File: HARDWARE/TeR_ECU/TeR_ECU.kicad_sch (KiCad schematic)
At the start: 6 parts

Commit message: Quick changes
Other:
- removed sheet ShutdownCircuit
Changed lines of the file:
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@@
-		)
-	)
-	(wire
-		(pts
-			(xy 83.82 149.86) (xy 83.82 151.13)
-		)
-		(stroke
-			(width 0)
-			(type default)
 		)
 	)
@@
 		(pts
 			(xy 157.48 120.65) (xy 170.18 120.65)
-		)
-		(stroke
-			(width 0)
-			(type default)
-		)
-	)
-	(wire
-		(pts
-			(xy 97.79 134.62) (xy 97.79 143.51)
 		)
 		(stroke
@@
 			(effects
 				(font
-					(size 1.27 1.27)
-				)
-				(justify left)
-			)
-		)
-		(instances
-			(project "TeR_ECU"
-				(path "/84413845-c4f3-4743-bcd2-a67649c90902"
-					(page "12")
-				)
-			)
-		)
-	)
-	(sheet
-		(at 83.82 143.51)
-		(size 17.78 20.32)
-		(fields_autoplaced yes)
-		(stroke
-			(width 0.1524)
-			(type solid)
-		)
-		(fill
-			(color 0 0 0 0.0000)
-		)
-		(property "Sheetname" "ShutdownCircuit"
-			(at 83.82 142.7984 0)
-			(effects
-				(font
-					(size 1.27 1.27)
-				)
-				(justify left bottom)
-			)
-		)
-		(property "Sheetfile" "safety_circuit.kicad_sch"
-			(at 83.82 164.4146 0)
-			(effects
-				(font
-					(size 1.27 1.27)
-				)
-				(justify left top)
-			)
-		)
-		(pin "SC" input
-			(at 97.79 143.51 90)
-			(effects
-				(font
-					(size 1.27 1.27)
-				)
-				(justify right)
-			)
-		)
-		(pin "safety_out" input
-			(at 83.82 147.32 180)
-			(effects
-				(font
-					(size 1.27 1.27)
-				)
-				(justify left)
-			)
-		)
-		(pin "safety_in" input
-			(at 83.82 151.13 180)
-			(effects
-				(font

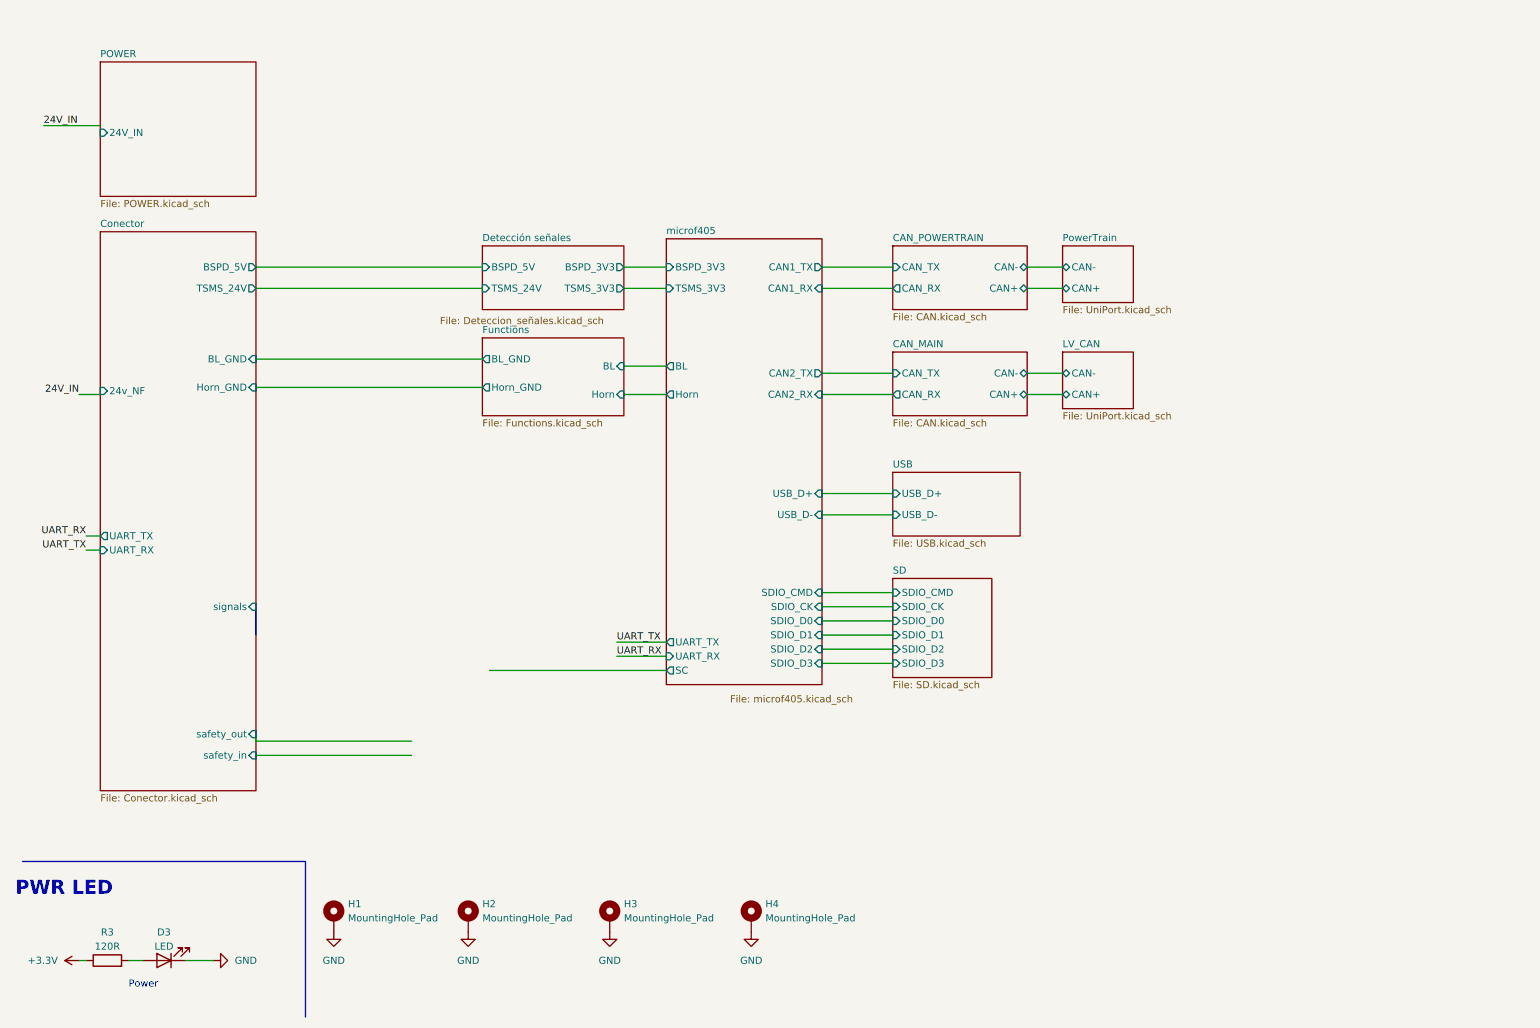
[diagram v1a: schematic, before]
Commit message: Advanced design and added IMU/GPS moduleç
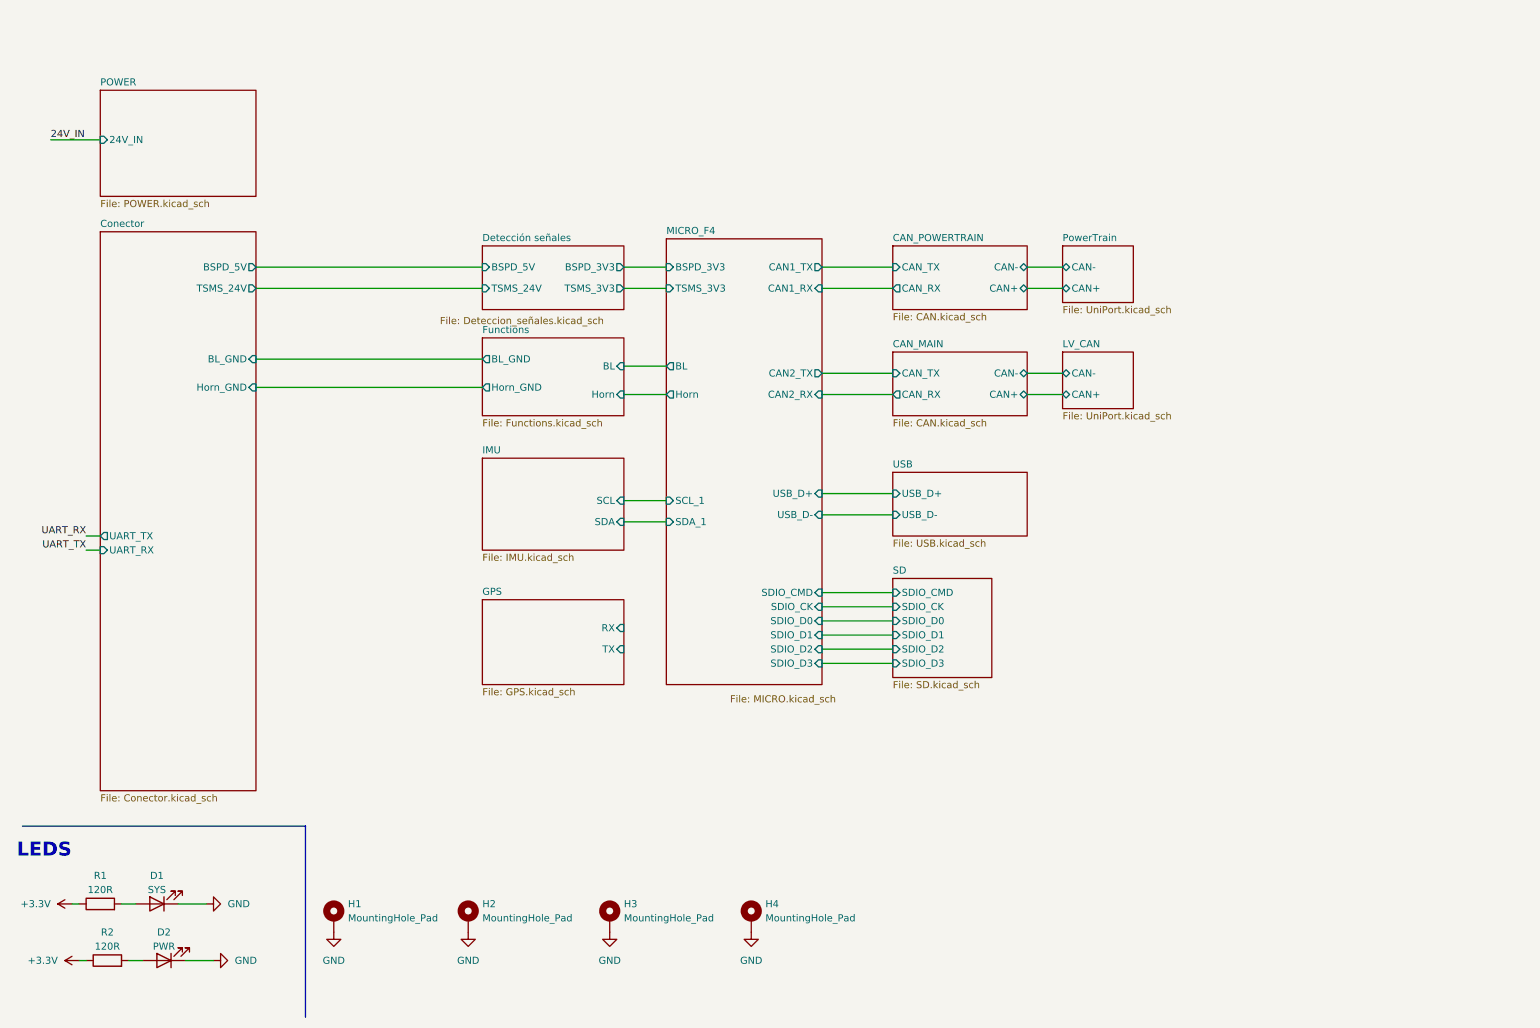
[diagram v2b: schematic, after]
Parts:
- added D1: SYS, LED_SMD:LED_0805_2012Metric, symbol Device:LED
- added R1: 120R, Resistor_SMD:R_0805_2012Metric, symbol Device:R
- D2: renamed from D3; value LED -> PWR
- renumbered R3 to R2
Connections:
- net +3.3V: now also R1.1
- net GND: now also D1.1 (K)
- new net: D1.2 (A), R1.2
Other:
- sheet microf405 renamed MICRO_F4
- added sheet GPS (GPS.kicad_sch)
- added sheet IMU (IMU.kicad_sch)
- sheet Conector ports: added none; removed 24v_NF, safety_in, safety_out, signals
- sheet MICRO_F4: file microf405.kicad_sch -> MICRO.kicad_sch
- sheet MICRO_F4 ports: added SCL_1, SDA_1; removed SC, UART_RX, UART_TX
- note added: "LEDS"
- note removed: "PWR LED"
- note removed: "Power"

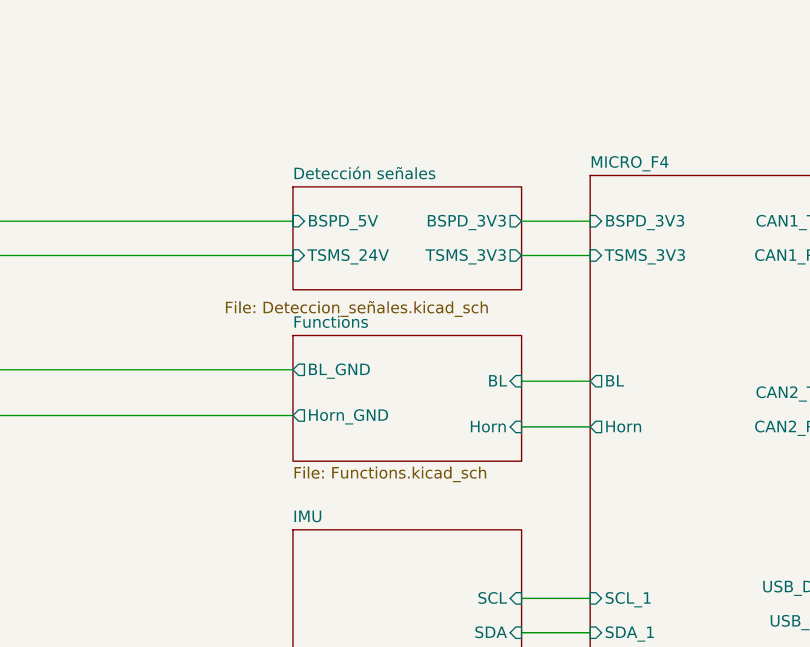
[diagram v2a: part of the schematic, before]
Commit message: Advanced RF fronted BIAS-T for LNA antenna and digital input redesign
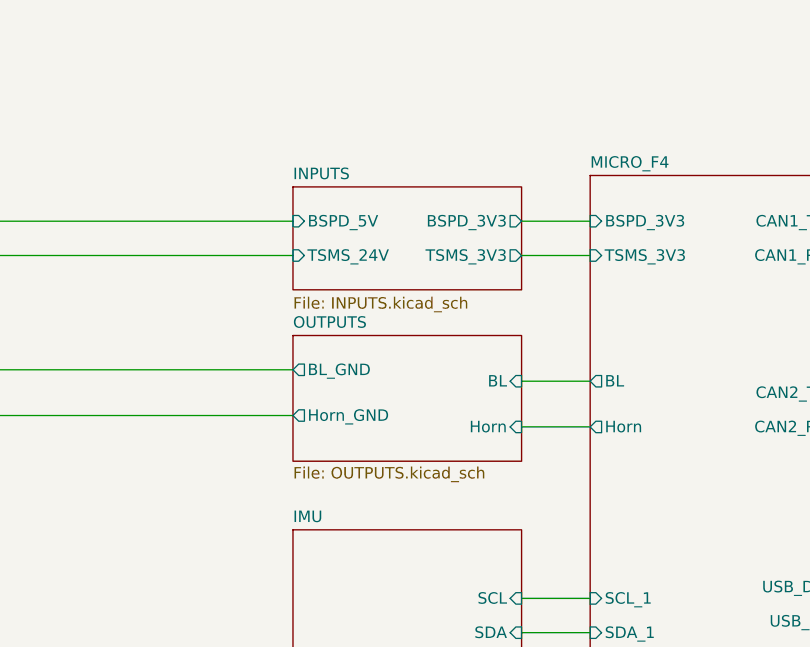
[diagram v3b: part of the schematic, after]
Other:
- sheet Detección señales renamed INPUTS
- sheet Functions renamed OUTPUTS
- sheet INPUTS: file Deteccion_señales.kicad_sch -> INPUTS.kicad_sch
- sheet OUTPUTS: file Functions.kicad_sch -> OUTPUTS.kicad_sch
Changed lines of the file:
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@@
 			(color 0 0 0 0.0000)
 		)
-		(property "Sheetname" "Functions"
+		(property "Sheetname" "OUTPUTS"
 			(at 96.52 74.2184 0)
 			(effects
@@
 			)
 		)
-		(property "Sheetfile" "Functions.kicad_sch"
+		(property "Sheetfile" "OUTPUTS.kicad_sch"
 			(at 96.52 89.4846 0)
 			(effects
@@
 			(color 0 0 0 0.0000)
 		)
-		(property "Sheetname" "Detección señales"
+		(property "Sheetname" "INPUTS"
 			(at 96.52 57.7084 0)
 			(effects
@@
 			)
 		)
-		(property "Sheetfile" "Deteccion_señales.kicad_sch"
-			(at 88.9 71.12 0)
-			(effects
-				(font
+		(property "Sheetfile" "INPUTS.kicad_sch"
+			(at 96.52 70.612 0)
+			(effects
+				(font

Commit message: Cool things
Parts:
- added D26: SYS, LED_SMD:LED_0805_2012Metric, symbol Device:LED
- added R13: 120R, Resistor_SMD:R_0805_2012Metric, symbol Device:R
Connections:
- net +3.3V: no longer R1.1
- net GND: now also D26.1 (K)
- new net: D26.2 (A), R13.2
- new net IMU_LED: R13.1
- new net SYS_LED: R1.1
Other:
- sheet OUTPUTS renamed D_OUTPUTS
- removed sheet SD
- added sheet EEPROM (EEPROM.kicad_sch)
- added sheet LEDS (WS2812.kicad_sch)
- added sheet PWM_OUT (PWM.kicad_sch)
- sheet Conector ports: added none; removed UART_RX, UART_TX
- sheet D_OUTPUTS ports: added DO0, DO1, DO2, DO3, DO4, DO5, DOUT0, DOUT1, DOUT2, DOUT3, DOUT4, DOUT5; removed BL, BL_GND, Horn, Horn_GND
- sheet INPUTS ports: added A0, A1, A2, A3, AIN0, AIN1, AIN2, AIN3, D0, D1, D2, D3, DIN0, DIN1, DIN2, DIN3; removed BSPD_3V3, BSPD_5V, TSMS_24V, TSMS_3V3
- sheet MICRO_F4 ports: added none; removed BL, Horn, SDIO_CK, SDIO_CMD, SDIO_D0, SDIO_D1, SDIO_D2, SDIO_D3
- sheet POWER ports: added none; removed 24V_IN
- moved on the sheet: D1, D2, R1, R2

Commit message: Quick changes, go to start layouting
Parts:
- added D1: SYS, LED_SMD:LED_0805_2012Metric, symbol Device:LED
- added IC1: MX34040NF2, MX34040NF2:MX34040NF2, symbol MX34040NF2:MX34040NF2
- added R1: 120R, Resistor_SMD:R_0805_2012Metric, symbol Device:R
- renumbered D26 to D2, D1 to D3, D2 to D4, R13 to R2, R1 to R3, R2 to R4
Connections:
- net GND: now also D1.1 (K)
- new net: D1.2 (A), R1.2
- new net ERR_LED: R1.1
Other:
- removed sheet Conector
- added sheet SC_RELAY (RELAY.kicad_sch)
- sheet D_OUTPUTS ports: added none; removed DO4, DO5, DOUT4, DOUT5
- sheet LEDS ports: added LED1, LED1_SPI, LED2, LED2_SPI; removed none
- sheet MICRO_F4 ports: added ADC1_0, ADC1_1, ADC1_2, ADC1_3, ERR_LED, IMU_LED, IN_0, IN_1, IN_2, IN_3, OUT_0, OUT_1, OUT_2, OUT_3, SCL_2, SC_EN, SDA_2, SPI1_MOSI, SPI2_MOSI, SYS_LED, T1_CH1, T1_CH2, T1_CH3, T1_CH4, UART_RX, UART_TX; removed BSPD_3V3, TSMS_3V3
- sheet PWM_OUT ports: added P0, P1, P2, P3, PWM0, PWM1, PWM2, PWM3; removed none

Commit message: Began layout
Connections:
- net +3.3V: now also IC1.21, IC1.22, IC1.23, IC1.24
- net 24_VIN: now also IC1.29, IC1.30, IC1.31, IC1.32
- net AIN0: now also IC1.1
- net AIN1: now also IC1.2
- net AIN2: now also IC1.3
- net AIN3: now also IC1.4
- net DIN0: now also IC1.5
- net DIN1: now also IC1.6
- net DIN2: now also IC1.7
- net DIN3: now also IC1.8
- net DOUT0: now also IC1.9
- net DOUT1: now also IC1.10
- net DOUT2: now also IC1.11
- net DOUT3: now also IC1.12
- net GND: now also IC1.33, IC1.34, IC1.35, IC1.36, IC1.37, IC1.38, IC1.39, IC1.40, IC1.41, IC1.42
- net LED1: now also IC1.17
- net LED2: now also IC1.18
- net PWM1: now also IC1.13
- net PWM2: now also IC1.14
- net PWM3: now also IC1.15
- net PWM4: now also IC1.16
- net SC_IN: now also IC1.19
- net SC_OUT: now also IC1.20
- net +5V: now reaches IC1.25
- net +5V: now also IC1.26, IC1.27, IC1.28
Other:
- moved on the sheet: IC1

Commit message: Finished layout, RF design, and quick DRC check, Lookin gud
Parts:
- D1: value SYS -> ERR
- D2: value SYS -> IMU
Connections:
- net PWM4 is gone; now on net PWM3: IC1.16
- net PWM1: now also IC1.14; no longer IC1.13
- net PWM2: now also IC1.15; no longer IC1.14
- net PWM3: no longer IC1.15
- net 24_VIN renamed +24V
- new net PWM0: IC1.13
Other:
- sheet MICRO_F4 ports: added T3_CH1, T3_CH2, T3_CH3, T3_CH4; removed T1_CH1, T1_CH2, T1_CH3, T1_CH4
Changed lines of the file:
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@@
 	(title_block
 		(title "TeR_ECU")
-		(date "2024-07-12")
+		(date "2024-11-03")
+		(rev "V2.0.0")
 		(company "Tecnun-eRacing")
 	)
@@
 	(wire
 		(pts
-			(xy 173.99 50.8) (xy 185.42 50.8)
-		)
-		(stroke
-			(width 0)
-			(type default)
-		)
-	)
-	(wire
-		(pts
 			(xy 63.5 60.96) (xy 63.5 63.5)
 		)
@@
 	(wire
 		(pts
-			(xy 140.97 87.63) (xy 148.59 87.63)
+			(xy 140.97 90.17) (xy 148.59 90.17)
 		)
 		(stroke
@@
 	(wire
 		(pts
-			(xy 140.97 90.17) (xy 148.59 90.17)
+			(xy 140.97 85.09) (xy 148.59 85.09)
 		)
 		(stroke
@@
 	(wire
 		(pts
-			(xy 140.97 85.09) (xy 148.59 85.09)
+			(xy 140.97 87.63) (xy 148.59 87.63)
 		)
 		(stroke
@@
 	(wire
 		(pts
+			(xy 173.99 53.34) (xy 185.42 53.34)
+		)
+		(stroke
+			(width 0)
+			(type default)
+		)
+	)
+	(wire
+		(pts
 			(xy 213.36 35.56) (xy 226.06 35.56)
 		)
@@
 	(wire
 		(pts
-			(xy 175.26 125.73) (xy 185.42 125.73)
+			(xy 173.99 50.8) (xy 185.42 50.8)
 		)
 		(stroke
@@
 	(wire
 		(pts
-			(xy 173.99 53.34) (xy 185.42 53.34)
+			(xy 175.26 125.73) (xy 185.42 125.73)
 		)
 		(stroke
@@
 	)
 	(label "PWM1"
-		(at 140.97 85.09 0)
+		(at 140.97 87.63 0)
 		(fields_autoplaced yes)
 		(effects
@@
 		)
 	)
-	(label "PWM3"
+	(label "PWM2"
 		(at 96.52 86.36 180)
 		(fields_autoplaced yes)
@@
 		)
 	)
-	(label "PWM4"
-		(at 140.97 92.71 0)
-		(fields_autoplaced yes)
-		(effects
-			(font
-				(size 1.27 1.27)
-			)
-			(justify left bottom)
-		)
-	)
 	(label "DOUT0"
 		(at 140.97 67.31 0)
@@
 		)
 	)
-	(label "PWM3"
-		(at 140.97 90.17 0)
-		(fields_autoplaced yes)
-		(effects
-			(font
-				(size 1.27 1.27)
-			)
-			(justify left bottom)
-		)
-	)
 	(label "DOUT1"
 		(at 140.97 69.85 0)
@@
 		)
 	)
-	(label "PWM4"
+	(label "PWM3"
 		(at 96.52 88.9 180)
 		(fields_autoplaced yes)
@@
 		)
 	)
+	(label "PWM3"
+		(at 140.97 92.71 0)
+		(fields_autoplaced yes)
+		(effects
+			(font
+				(size 1.27 1.27)
+			)
+			(justify left bottom)
+		)
+	)
 	(label "AIN2"
 		(at 96.52 55.88 180)
@@
 		)
 	)
-	(label "PWM1"
+	(label "PWM0"
 		(at 96.52 81.28 180)
 		(fields_autoplaced yes)
@@
 	)
 	(label "PWM2"
-		(at 140.97 87.63 0)
+		(at 140.97 90.17 0)
 		(fields_autoplaced yes)
 		(effects
@@
 		)
 	)
-	(label "PWM2"
+	(label "PWM1"
 		(at 96.52 83.82 180)
 		(fields_autoplaced yes)
@@
 		)
 	)
-	(label "AIN0"
-		(at 140.97 48.26 0)
+	(label "PWM0"
+		(at 140.97 85.09 0)
 		(fields_autoplaced yes)
 		(effects
@@
 		)
 	)
-	(label "DIN1"
-		(at 140.97 36.83 0)
+	(label "AIN0"
+		(at 140.97 48.26 0)
 		(fields_autoplaced yes)
 		(effects
@@
 		)
 	)
-	(label "LED2"
-		(at 140.97 105.41 0)
+	(label "DIN1"
+		(at 140.97 36.83 0)
 		(fields_autoplaced yes)
 		(effects
@@
 		)
 	)
-	(global_label "24_VIN"
-		(shape input)
-		(at 59.69 71.12 180)
+	(label "LED2"
+		(at 140.97 105.41 0)
 		(fields_autoplaced yes)
 		(effects
@@
 				(size 1.27 1.27)
 			)
-			(justify right)
-		)
-		(property "Intersheetrefs" "${INTERSHEET_REFS}"
-			(at 50.2943 71.12 0)
-			(effects
-				(font
-					(size 1.27 1.27)
-				)
-				(justify right)
-				(hide yes)
-			)
+			(justify left bottom)
 		)
 	)
@@
 	)
 	(symbol
+		(lib_id "power:+24V")
+		(at 59.69 71.12 90)
+		(unit 1)
+		(exclude_from_sim no)
+		(in_bom yes)
+		(on_board yes)
+		(dnp no)
+		(fields_autoplaced yes)
+		(property "Reference" "#PWR0141"
+			(at 63.5 71.12 0)
+			(effects
+				(font
+					(size 1.27 1.27)
+				)
+				(hide yes)
+			)
+		)
+		(property "Value" "+24V"
+			(at 55.88 71.1199 90)
+			(effects
+				(font
+					(size 1.27 1.27)
+				)
+				(justify left)
+			)
+		)
+		(property "Footprint" ""
+			(at 59.69 71.12 0)
+			(effects
+				(font
+					(size 1.27 1.27)
+				)
+				(hide yes)
+			)
+		)
+		(property "Datasheet" ""
+			(at 59.69 71.12 0)
+			(effects
+				(font
+					(size 1.27 1.27)
+				)
+				(hide yes)
+			)
+		)
+		(property "Description" "Power symbol creates a global label with name \"+24V\""
+			(at 59.69 71.12 0)
+			(effects
+				(font
+					(size 1.27 1.27)
+				)
+				(hide yes)
+			)
+		)
+		(pin "1"
+		)
+		(instances
+			(project ""
+				(path "/84413845-c4f3-4743-bcd2-a67649c90902"
+					(reference "#PWR0141")
+					(unit 1)
+				)
+			)
+		)
+	)
+	(symbol
 		(lib_id "Device:R")
 		(at 30.48 179.07 90)
@@
 			)
 		)
-		(property "Value" "SYS"
+		(property "Value" "ERR"
 			(at 40.64 168.91 0)
 			(effects
@@
 			)
 		)
-		(property "Value" "SYS"
+		(property "Value" "IMU"
 			(at 40.64 176.53 0)
 			(effects
@@
 			)
 		)
-		(pin "T1_CH2" input
-			(at 185.42 87.63 180)
+		(pin "SPI2_MOSI" input
+			(at 185.42 105.41 180)
 			(effects
 				(font
@@
 			)
 		)
-		(pin "T1_CH3" input
-			(at 185.42 90.17 180)
+		(pin "SPI1_MOSI" input
+			(at 185.42 102.87 180)
 			(effects
 				(font
@@
 			)
 		)
-		(pin "T1_CH4" input
-			(at 185.42 92.71 180)
+		(pin "OUT_1" input
+			(at 185.42 69.85 180)
 			(effects
 				(font
@@
 			)
 		)
-		(pin "T1_CH1" input
-			(at 185.42 85.09 180)
+		(pin "OUT_2" input
+			(at 185.42 72.39 180)
 			(effects
 				(font
@@
 			)
 		)
-		(pin "SPI2_MOSI" input
-			(at 185.42 105.41 180)
+		(pin "OUT_0" input
+			(at 185.42 67.31 180)
 			(effects
 				(font
@@
 			)
 		)
-		(pin "SPI1_MOSI" input
-			(at 185.42 102.87 180)
+		(pin "OUT_3" input
+			(at 185.42 74.93 180)
 			(effects
 				(font
@@
 			)
 		)
-		(pin "OUT_1" input
-			(at 185.42 69.85 180)
+		(pin "SC_EN" input
+			(at 185.42 118.11 180)
 			(effects
 				(font
@@
 			)
 		)
-		(pin "OUT_2" input
-			(at 185.42 72.39 180)
+		(pin "ERR_LED" input
+			(at 185.42 128.27 180)
 			(effects
 				(font
@@
 			)
 		)
-		(pin "OUT_0" input
-			(at 185.42 67.31 180)
+		(pin "SYS_LED" input
+			(at 185.42 125.73 180)
 			(effects
 				(font
@@
 			)
 		)
-		(pin "OUT_3" input
-			(at 185.42 74.93 180)
+		(pin "IMU_LED" input
+			(at 185.42 130.81 180)
 			(effects
 				(font
@@
 			)
 		)
-		(pin "SC_EN" input
-			(at 185.42 118.11 180)
+		(pin "T3_CH1" input
+			(at 185.42 85.09 180)
 			(effects
 				(font
@@
 			)
 		)
-		(pin "ERR_LED" input
-			(at 185.42 128.27 180)
+		(pin "T3_CH2" input
+			(at 185.42 87.63 180)
 			(effects
 				(font
@@
 			)
 		)
-		(pin "SYS_LED" input
-			(at 185.42 125.73 180)
+		(pin "T3_CH3" input
+			(at 185.42 90.17 180)
 			(effects
 				(font
@@
 			)
 		)
-		(pin "IMU_LED" input
-			(at 185.42 130.81 180)
+		(pin "T3_CH4" input
+			(at 185.42 92.71 180)
 			(effects
 				(font
@@
 		)
 		(pin "PWM1" input
-			(at 148.59 85.09 180)
+			(at 148.59 87.63 180)
 			(effects
 				(font
@@
 		)
 		(pin "PWM0" input
-			(at 148.59 90.17 180)
+			(at 148.59 85.09 180)
 			(effects
 				(font
@@
 		)
 		(pin "PWM2" input
-			(at 148.59 87.63 180)
+			(at 148.59 90.17 180)
 			(effects
 				(font
